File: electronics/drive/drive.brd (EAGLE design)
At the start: 35 x 25 mm, 11 parts, among them IC1 MEGA8-AI, IC2 MAX1483ESA, J1 AVR_SPI_PRG_6NS

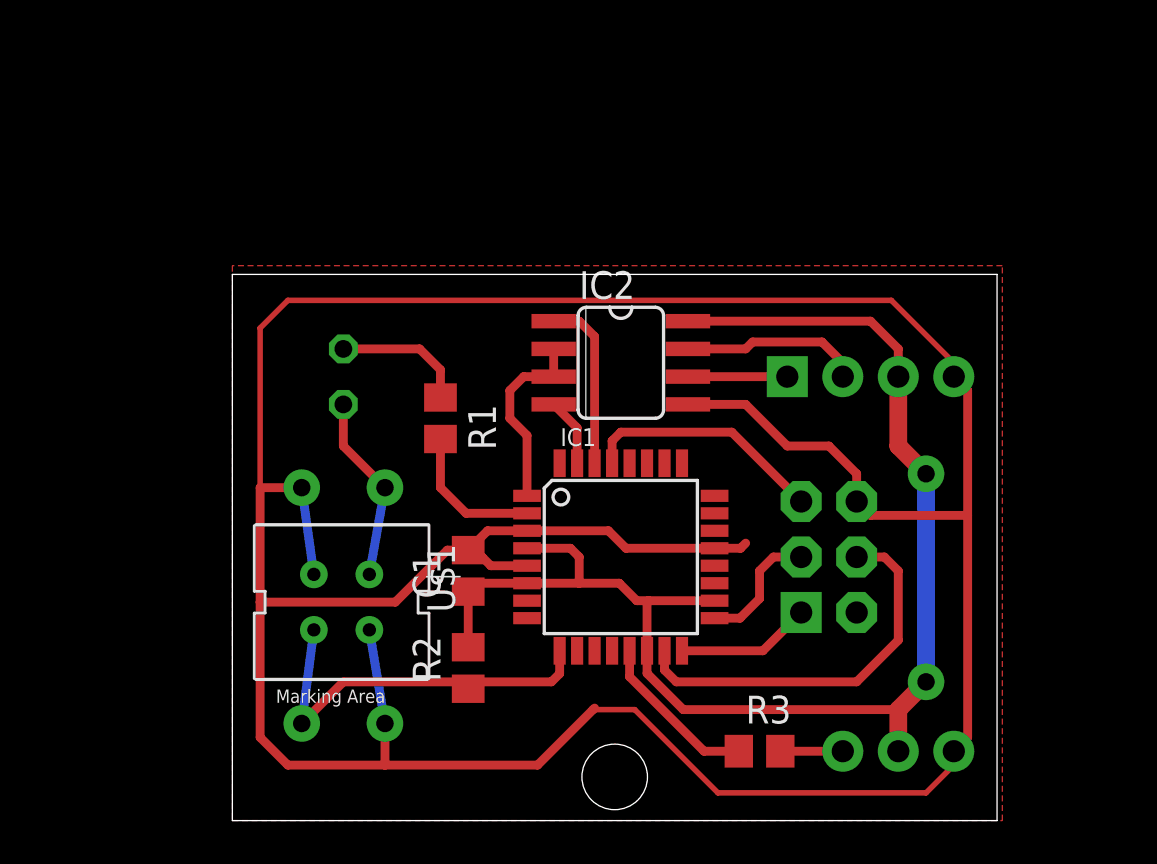
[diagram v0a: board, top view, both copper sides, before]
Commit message: Fixing a bug in drive board design.
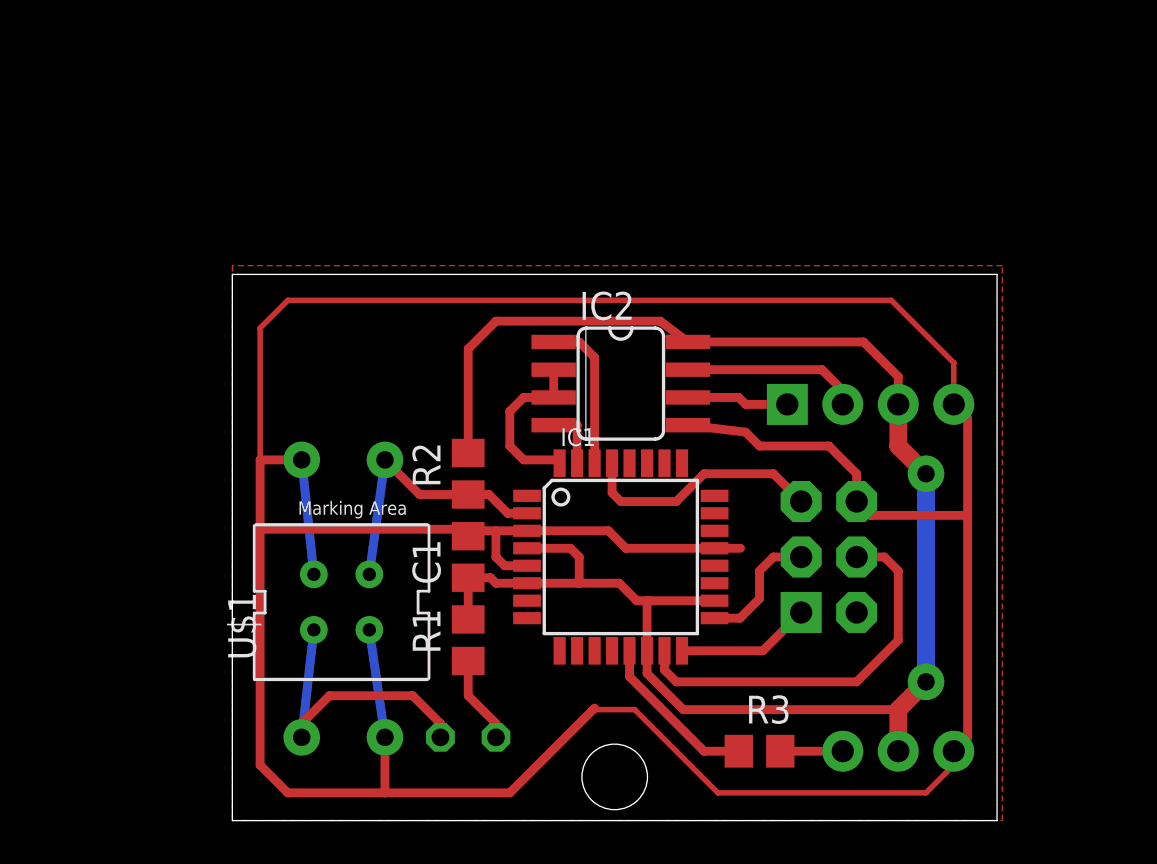
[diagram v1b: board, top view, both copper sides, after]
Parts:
- moved LED1 17.5 mm to (10.8, 3.81), turned to 0 degrees
- moved R1 10.2 mm to (10.8, 8.26), turned to 90 degrees
- moved R2 8.89 mm to (10.8, 15.9)
- moved JP1 1.27 mm to (25.4, 19.1)
- moved IC2 0.95 mm to (17.8, 20.0)
- moved C1 0.63 mm to (10.8, 12.1)
- turned U$1 to 90 degrees
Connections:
- removed net SENSOR_POWER: IC1.2, R1.2
- net +5V: now also R1.2
- net SENSOR: now also IC1.2; no longer IC1.9
- net TXEN: now also IC1.32; no longer IC1.1
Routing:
- net +5V: track 64.7 -> 78.0 mm
- net SENSOR_POWER: track 6.67 -> 0.00 mm
- net SENSOR: track 18.4 -> 12.8 mm
- net N$2: track 8.63 -> 13.6 mm
- net GND: track 161.5 -> 163.8 mm
- net N$3: track 6.11 -> 4.02 mm
- net TXEN: track 8.69 -> 7.73 mm
- net RX: track 7.96 -> 7.01 mm

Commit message: More fiddling with drive board.
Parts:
- moved J1 0.63 mm to (26.7, 12.1)
- moved JP1 0.63 mm to (25.4, 19.7)
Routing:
- net +5V: track 78.0 -> 80.3 mm
- net D-: track 8.12 -> 9.01 mm
- net RESET: track 11.2 -> 10.6 mm
- net MISO: track 6.18 -> 5.55 mm
- net MOSI: track 17.9 -> 18.6 mm
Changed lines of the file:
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@@
 <element name="R1" library="rcl" package="R0805" value="200" x="10.795" y="8.255" rot="R90"/>
 <element name="C1" library="rcl" package="C0805" value="100nF" x="10.795" y="12.065" rot="R90"/>
-<element name="JP1" library="SparkFun" package="MOLEX-1X4" value="" x="25.4" y="19.05" rot="MR180"/>
+<element name="JP1" library="SparkFun" package="MOLEX-1X4" value="" x="25.4" y="19.685" rot="MR180"/>
 <element name="JP2" library="SparkFun" package="1X03" value="" x="33.02" y="3.175" rot="MR0"/>
 <element name="IC1" library="atmel" package="TQFP32-08" value="MEGA8-AI" x="17.78" y="12.065">
@@
 <attribute name="OC_NEWARK" value="90C3817" x="17.78" y="20.0025" size="1.778" layer="27" rot="R270" display="off"/>
 </element>
-<element name="J1" library="SparkFun" package="2X3-NS" value="AVR_SPI_PRG_6NS" x="27.305" y="12.065" rot="MR90"/>
+<element name="J1" library="SparkFun" package="2X3-NS" value="AVR_SPI_PRG_6NS" x="26.67" y="12.065" rot="MR90"/>
 <element name="R2" library="rcl" package="R0805" value="12k" x="10.795" y="15.875" rot="R90"/>
 <element name="R3" library="rcl" package="R0805" value="1k" x="24.13" y="3.175"/>
@@
 <wire x1="18.415" y1="5.08" x2="22.225" y2="1.27" width="0.254" layer="1"/>
 <wire x1="16.51" y1="5.08" x2="18.415" y2="5.08" width="0.254" layer="1"/>
-<wire x1="33.02" y1="20.955" x2="33.02" y2="19.05" width="0.254" layer="1"/>
+<wire x1="33.02" y1="20.955" x2="33.02" y2="19.685" width="0.254" layer="1"/>
 <wire x1="30.1625" y1="23.8125" x2="33.02" y2="20.955" width="0.254" layer="1"/>
 <wire x1="2.54" y1="23.8125" x2="30.1625" y2="23.8125" width="0.254" layer="1"/>
@@
 <wire x1="33.655" y1="3.81" x2="33.655" y2="13.97" width="0.4064" layer="1"/>
 <wire x1="33.655" y1="13.97" x2="33.655" y2="18.415" width="0.4064" layer="1"/>
-<wire x1="33.655" y1="18.415" x2="33.02" y2="19.05" width="0.4064" layer="1"/>
-<wire x1="23.495" y1="17.78" x2="24.13" y2="17.145" width="0.4064" layer="1"/>
-<wire x1="24.13" y1="17.145" x2="27.305" y2="17.145" width="0.4064" layer="1"/>
-<wire x1="27.305" y1="17.145" x2="28.575" y2="15.875" width="0.4064" layer="1"/>
-<wire x1="28.575" y1="15.875" x2="28.575" y2="14.605" width="0.4064" layer="1"/>
-<wire x1="28.575" y1="14.605" x2="29.21" y2="13.97" width="0.4064" layer="1"/>
-<wire x1="29.21" y1="13.97" x2="33.655" y2="13.97" width="0.4064" layer="1"/>
+<wire x1="33.655" y1="18.415" x2="33.02" y2="19.685" width="0.4064" layer="1"/>
 <wire x1="13.4874" y1="11.665" x2="12.465" y2="11.665" width="0.4064" layer="1"/>
 <wire x1="12.465" y1="11.665" x2="12.065" y2="12.065" width="0.4064" layer="1"/>
@@
 <wire x1="11.045" y1="13.265" x2="10.795" y2="13.015" width="0.4064" layer="1"/>
 <wire x1="10.795" y1="13.335" x2="10.795" y2="13.015" width="0.4064" layer="1"/>
-<wire x1="23.495" y1="17.78" x2="20.8534" y2="18.0975" width="0.4064" layer="1"/>
 <wire x1="22.0726" y1="12.465" x2="23.26" y2="12.465" width="0.4064" layer="1"/>
 <wire x1="22.0726" y1="12.465" x2="18.015" y2="12.465" width="0.4064" layer="1"/>
+<wire x1="20.8534" y1="18.0975" x2="23.1775" y2="18.0975" width="0.4064" layer="1"/>
+<wire x1="23.1775" y1="18.0975" x2="24.13" y2="17.145" width="0.4064" layer="1"/>
+<wire x1="24.13" y1="17.145" x2="27.305" y2="17.145" width="0.4064" layer="1"/>
+<wire x1="27.305" y1="17.145" x2="27.94" y2="16.51" width="0.4064" layer="1"/>
+<wire x1="27.94" y1="16.51" x2="27.94" y2="14.605" width="0.4064" layer="1"/>
+<wire x1="27.94" y1="14.605" x2="28.575" y2="13.97" width="0.4064" layer="1"/>
+<wire x1="28.575" y1="13.97" x2="33.655" y2="13.97" width="0.4064" layer="1"/>
 </signal>
 <signal name="SENSOR">
@@
 <wire x1="19.05" y1="10.065" x2="18.98" y2="9.995" width="0.4064" layer="1"/>
 <wire x1="30.48" y1="4.1275" x2="30.48" y2="3.175" width="0.4064" layer="1"/>
-<wire x1="30.48" y1="19.05" x2="30.48" y2="20.32" width="0.4064" layer="1"/>
+<wire x1="30.48" y1="19.685" x2="30.48" y2="20.32" width="0.4064" layer="1"/>
 <wire x1="18.98" y1="7.7724" x2="18.98" y2="6.7375" width="0.4064" layer="1"/>
 <via x="31.75" y="6.35" extent="1-16" drill="0.8" diameter="1.6764"/>
-<wire x1="31.75" y1="15.875" x2="31.75" y2="6.35" width="0.8128" layer="16"/>
+<wire x1="31.75" y1="15.875" x2="31.75" y2="6.35" width="1.016" layer="16"/>
 <via x="31.75" y="15.875" extent="1-16" drill="0.8" diameter="1.6764"/>
 <wire x1="18.98" y1="6.7375" x2="20.6375" y2="5.08" width="0.4064" layer="1"/>
-<wire x1="30.48" y1="5.08" x2="30.48" y2="3.175" width="0.8128" layer="1"/>
-<wire x1="31.75" y1="6.35" x2="30.48" y2="5.08" width="0.8128" layer="1"/>
-<wire x1="30.48" y1="19.05" x2="30.48" y2="17.145" width="0.8128" layer="1"/>
-<wire x1="30.48" y1="17.145" x2="31.75" y2="15.875" width="0.8128" layer="1"/>
+<wire x1="30.48" y1="5.08" x2="30.48" y2="3.175" width="1.016" layer="1"/>
+<wire x1="31.75" y1="6.35" x2="30.48" y2="5.08" width="1.016" layer="1"/>
+<wire x1="30.48" y1="19.685" x2="30.48" y2="17.145" width="1.016" layer="1"/>
+<wire x1="30.48" y1="17.145" x2="31.75" y2="15.875" width="1.016" layer="1"/>
 <contactref element="R1" pad="2"/>
 <wire x1="13.4874" y1="10.865" x2="12.065" y2="10.865" width="0.4064" layer="1"/>
@@
 <wire x1="12.065" y1="22.86" x2="10.795" y2="21.59" width="0.4064" layer="1"/>
 <wire x1="10.795" y1="21.59" x2="10.795" y2="16.825" width="0.4064" layer="1"/>
-<wire x1="12.065" y1="22.86" x2="19.5834" y2="22.86" width="0.4064" layer="1"/>
-<wire x1="19.5834" y1="22.86" x2="20.8534" y2="21.9075" width="0.4064" layer="1"/>
-<wire x1="30.48" y1="20.32" x2="28.8925" y2="21.9075" width="0.4064" layer="1"/>
-<wire x1="20.8534" y1="21.9075" x2="28.8925" y2="21.9075" width="0.4064" layer="1"/>
+<wire x1="12.065" y1="22.86" x2="17.78" y2="22.86" width="0.4064" layer="1"/>
+<wire x1="17.78" y1="22.86" x2="18.7325" y2="21.9075" width="0.4064" layer="1"/>
+<wire x1="20.8534" y1="21.9075" x2="18.7325" y2="21.9075" width="0.4064" layer="1"/>
+<wire x1="20.8534" y1="21.9075" x2="22.5425" y2="21.9075" width="0.4064" layer="1"/>
+<wire x1="22.5425" y1="21.9075" x2="23.495" y2="22.86" width="0.4064" layer="1"/>
+<wire x1="23.495" y1="22.86" x2="29.21" y2="22.86" width="0.4064" layer="1"/>
+<wire x1="29.21" y1="22.86" x2="30.48" y2="21.59" width="0.4064" layer="1"/>
+<wire x1="30.48" y1="21.59" x2="30.48" y2="19.685" width="0.4064" layer="1"/>
 </signal>
 <signal name="SERVO">
@@
 <contactref element="J1" pad="3"/>
 <wire x1="22.0726" y1="9.265" x2="23.235" y2="9.265" width="0.4064" layer="1"/>
-<wire x1="23.235" y1="9.265" x2="24.13" y2="10.16" width="0.4064" layer="1"/>
-<wire x1="24.13" y1="10.16" x2="24.13" y2="11.43" width="0.4064" layer="1"/>
-<wire x1="24.13" y1="11.43" x2="24.765" y2="12.065" width="0.4064" layer="1"/>
-<wire x1="24.765" y1="12.065" x2="26.035" y2="12.065" width="0.4064" layer="1"/>
+<wire x1="23.235" y1="9.265" x2="23.495" y2="9.525" width="0.4064" layer="1"/>
+<wire x1="23.495" y1="9.525" x2="23.495" y2="11.43" width="0.4064" layer="1"/>
+<wire x1="23.495" y1="11.43" x2="24.13" y2="12.065" width="0.4064" layer="1"/>
+<wire x1="24.13" y1="12.065" x2="25.4" y2="12.065" width="0.4064" layer="1"/>
 </signal>
 <signal name="MISO">
 <contactref element="IC1" pad="16"/>
 <contactref element="J1" pad="1"/>
-<wire x1="20.58" y1="7.7724" x2="24.2824" y2="7.7724" width="0.4064" layer="1"/>
-<wire x1="24.2824" y1="7.7724" x2="26.035" y2="9.525" width="0.4064" layer="1"/>
+<wire x1="20.58" y1="7.7724" x2="23.6474" y2="7.7724" width="0.4064" layer="1"/>
+<wire x1="23.6474" y1="7.7724" x2="25.4" y2="9.525" width="0.4064" layer="1"/>
 </signal>
 <signal name="MOSI">
@@
 <wire x1="30.48" y1="8.255" x2="30.48" y2="11.43" width="0.4064" layer="1"/>
 <wire x1="30.48" y1="11.43" x2="29.845" y2="12.065" width="0.4064" layer="1"/>
-<wire x1="29.845" y1="12.065" x2="28.575" y2="12.065" width="0.4064" layer="1"/>
+<wire x1="29.845" y1="12.065" x2="27.94" y2="12.065" width="0.4064" layer="1"/>
 </signal>
 <signal name="RESET">
@@
 <wire x1="17.78" y1="14.605" x2="20.32" y2="14.605" width="0.4064" layer="1"/>
 <wire x1="20.32" y1="14.605" x2="21.59" y2="15.875" width="0.4064" layer="1"/>
-<wire x1="21.59" y1="15.875" x2="24.765" y2="15.875" width="0.4064" layer="1"/>
-<wire x1="24.765" y1="15.875" x2="26.035" y2="14.605" width="0.4064" layer="1"/>
+<wire x1="21.59" y1="15.875" x2="24.13" y2="15.875" width="0.4064" layer="1"/>
+<wire x1="24.13" y1="15.875" x2="25.4" y2="14.605" width="0.4064" layer="1"/>
 </signal>
 <signal name="D+">
@@
 <contactref element="JP1" pad="1"/>
 <wire x1="20.8534" y1="19.3675" x2="23.1775" y2="19.3675" width="0.4064" layer="1"/>
-<wire x1="23.1775" y1="19.3675" x2="23.495" y2="19.05" width="0.4064" layer="1"/>
-<wire x1="23.495" y1="19.05" x2="25.4" y2="19.05" width="0.4064" layer="1"/>
+<wire x1="23.1775" y1="19.3675" x2="23.495" y2="19.685" width="0.4064" layer="1"/>
+<wire x1="23.495" y1="19.685" x2="25.4" y2="19.685" width="0.4064" layer="1"/>
 </signal>
 <signal name="D-">
 <contactref element="IC2" pad="7"/>
 <contactref element="JP1" pad="2"/>
-<wire x1="20.8534" y1="20.6375" x2="26.9875" y2="20.6375" width="0.4064" layer="1"/>
-<wire x1="26.9875" y1="20.6375" x2="27.94" y2="19.685" width="0.4064" layer="1"/>
-<wire x1="27.94" y1="19.685" x2="27.94" y2="19.05" width="0.4064" layer="1"/>
+<wire x1="20.8534" y1="20.6375" x2="22.5425" y2="20.6375" width="0.4064" layer="1"/>
+<wire x1="22.5425" y1="20.6375" x2="23.495" y2="21.59" width="0.4064" layer="1"/>
+<wire x1="23.495" y1="21.59" x2="27.305" y2="21.59" width="0.4064" layer="1"/>
+<wire x1="27.305" y1="21.59" x2="27.94" y2="20.955" width="0.4064" layer="1"/>
+<wire x1="27.94" y1="20.955" x2="27.94" y2="19.685" width="0.4064" layer="1"/>
 </signal>
 <signal name="TXEN">
@@
 </signal>
 </signals>
-<errors>
-</errors>
 </board>
 </drawing>

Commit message: Final modifications of the drive board.
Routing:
- net GND: track 164.2 -> 163.3 mm
